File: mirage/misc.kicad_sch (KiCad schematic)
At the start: 6 parts

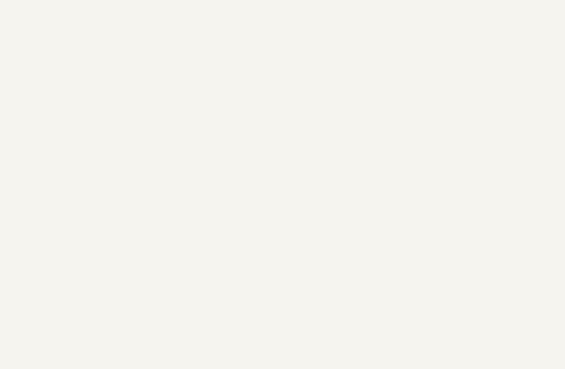
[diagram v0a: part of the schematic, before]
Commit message: feat: add big buzzer
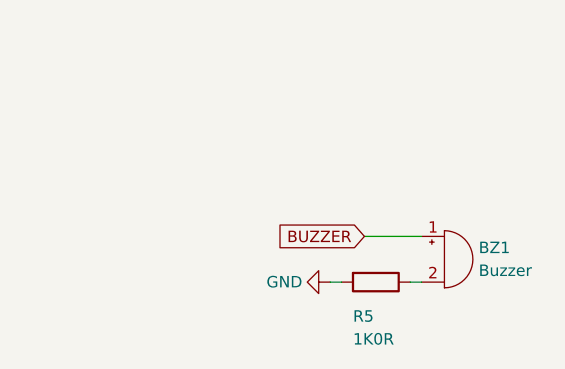
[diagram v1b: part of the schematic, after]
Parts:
- added BZ1: Buzzer, symbol Device:Buzzer
- added R5: 1K0R, Resistor_SMD:R_0402_1005Metric, symbol Device:R
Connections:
- net GND: now also R5.2
- new net: BZ1.2 (-), R5.1
- new net BUZZER: BZ1.1 (+)

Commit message: revert: remove testing
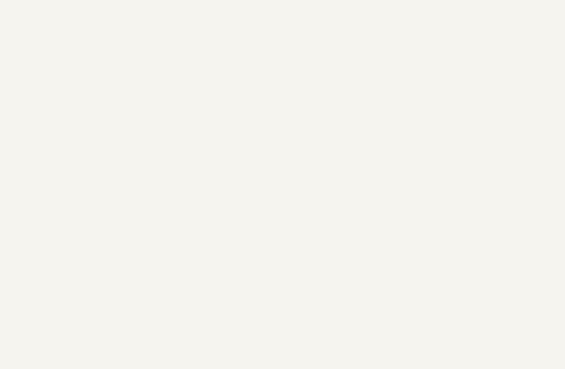
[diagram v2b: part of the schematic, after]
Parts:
- removed BZ1: Buzzer, symbol Device:Buzzer
- removed R5: 1K0R, Resistor_SMD:R_0402_1005Metric, symbol Device:R
